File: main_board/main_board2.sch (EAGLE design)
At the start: 16 parts, among them J1 Bar30, J2 Temp/Hum, J3 LED, Q1 MOSFET, Q2 MOSFET, Q3 MOSFET

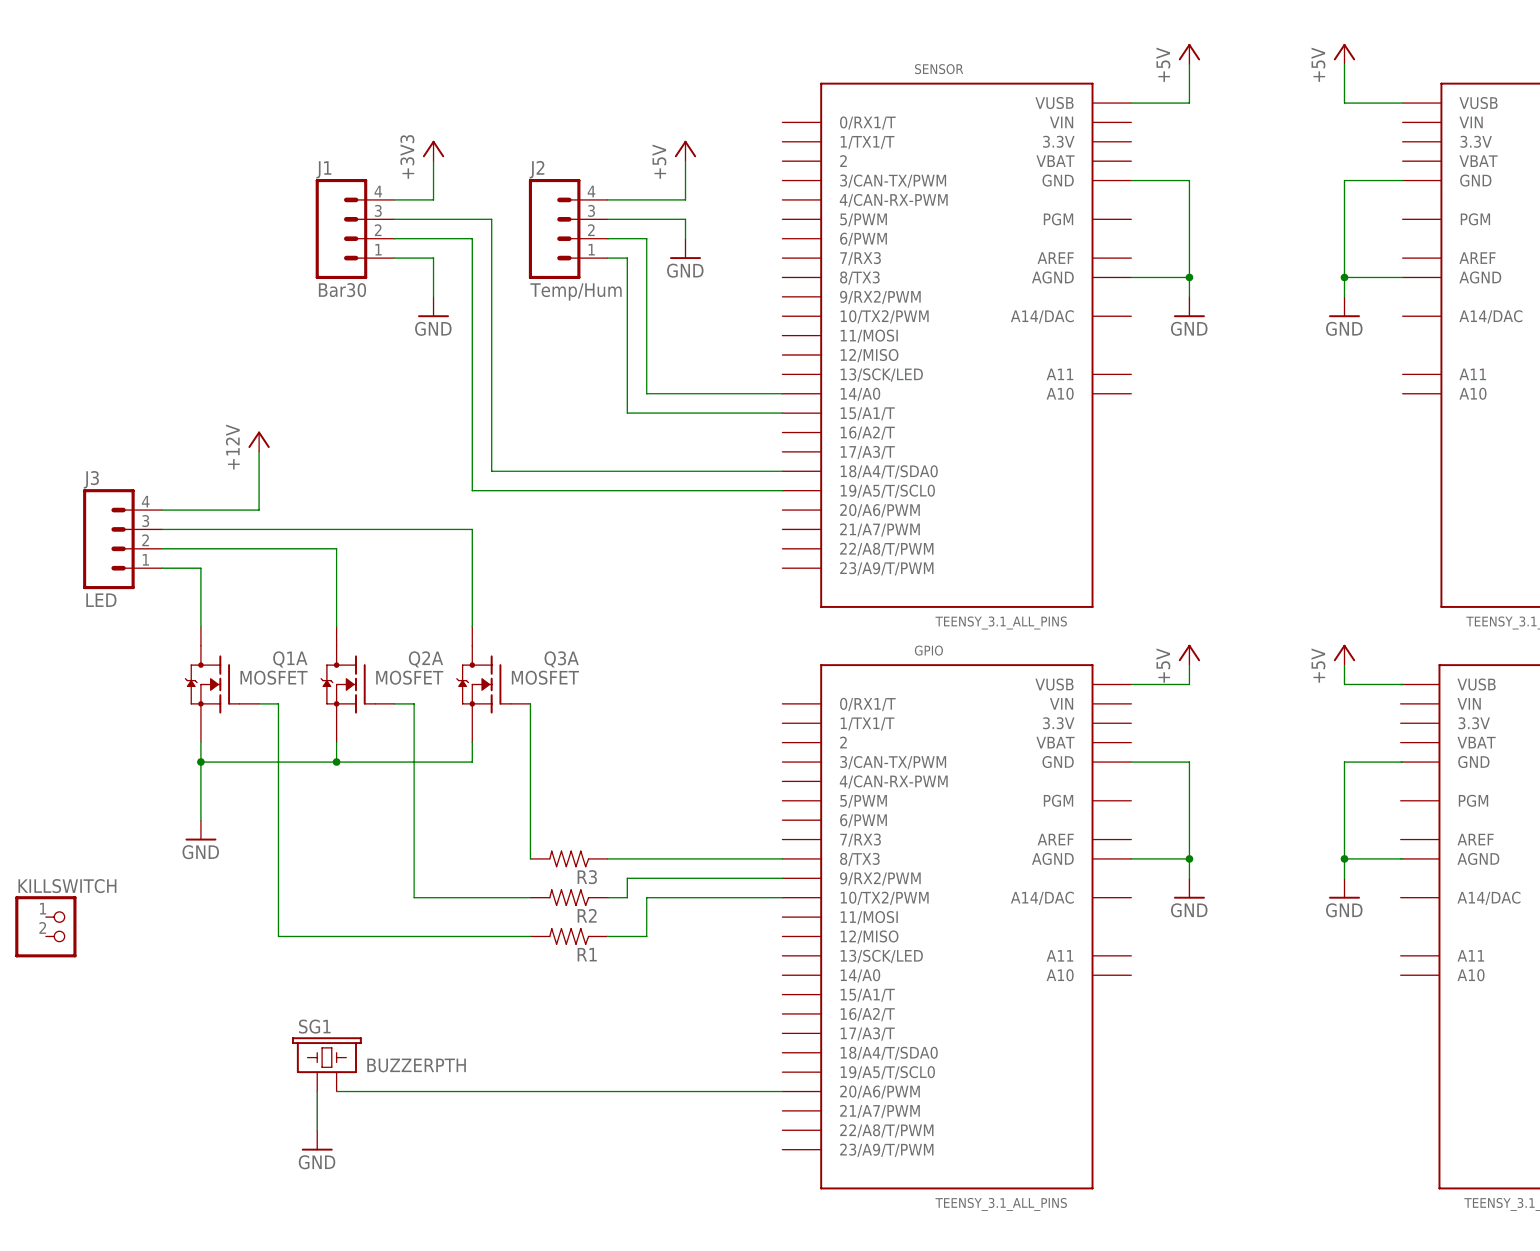
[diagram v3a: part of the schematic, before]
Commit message: added kill switch. moved minor parts around. added 3.3V references
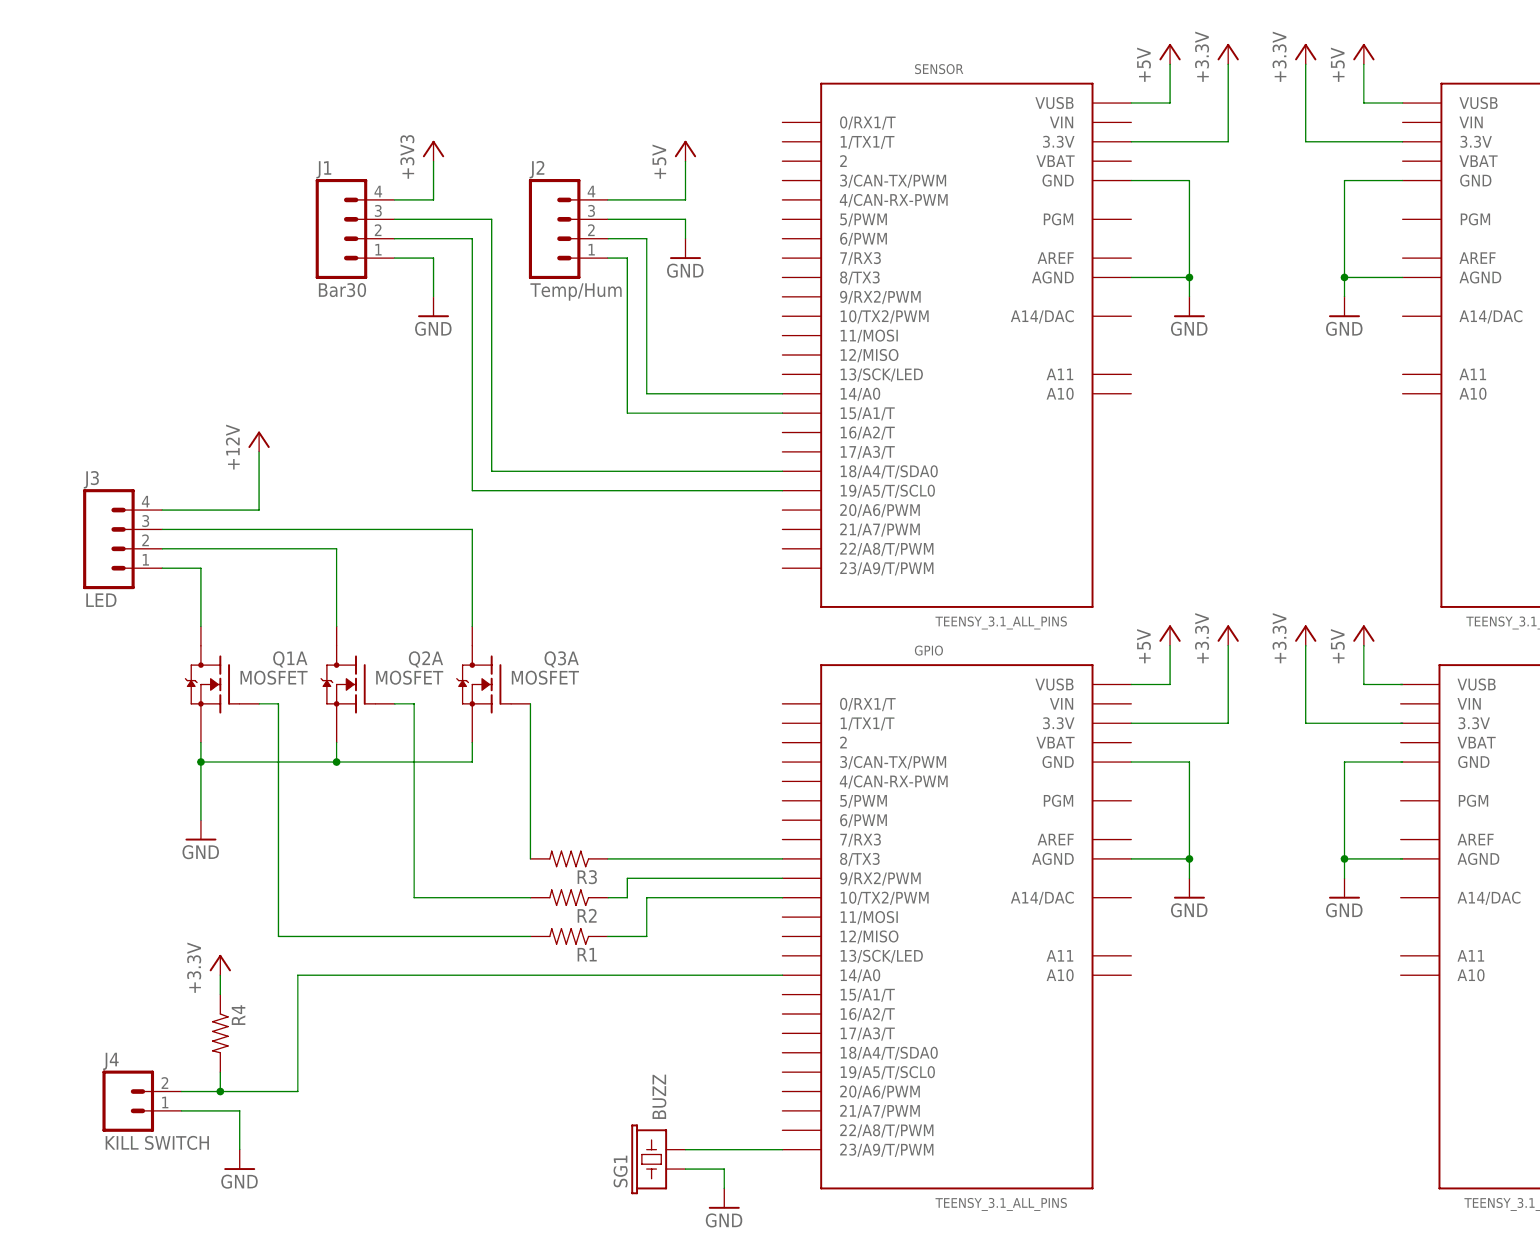
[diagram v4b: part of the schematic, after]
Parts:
- removed KILLSWITCH: (no value), pinhead:PINHD-1X2
- added J4: KILL SWITCH, SparkFun-Connectors:M02PTH
- added R4: (no value), SparkFun-Resistors:RESISTORPTH-1/4W
- SG1: value BUZZERPTH -> BUZZ
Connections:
- new net N$20: GPIO.14/A0, J4.2, R4.2
- net +5V: now also GPIO.3.3V, POWER.3.3V, R4.1, SENSOR.3.3V
- net GND: now also J4.1
- net N$13: now also GPIO.23/A9/T/PWM; no longer GPIO.20/A6/PWM
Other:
- moved on the sheet: SG1
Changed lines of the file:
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@@
 <part name="GND1" library="supply1" deviceset="GND" device=""/>
 <part name="P+1" library="supply1" deviceset="+5V" device=""/>
-<part name="KILLSWITCH" library="pinhead" deviceset="PINHD-1X2" device=""/>
 <part name="J1" library="SparkFun-Connectors" deviceset="M04" device="PTH" value="Bar30"/>
-<part name="SG1" library="SparkFun-Electromechanical" deviceset="BUZZER" device="PTH"/>
+<part name="SG1" library="SparkFun-Electromechanical" deviceset="BUZZER" device="PTH" value="BUZZ"/>
 <part name="GND2" library="SparkFun-Aesthetics" deviceset="GND" device=""/>
 <part name="GND3" library="SparkFun-Aesthetics" deviceset="GND" device=""/>
@@
 <part name="GND7" library="supply1" deviceset="GND" device=""/>
 <part name="GND8" library="supply1" deviceset="GND" device=""/>
+<part name="J4" library="SparkFun-Connectors" deviceset="M02" device="PTH" value="KILL SWITCH"/>
+<part name="R4" library="SparkFun-Resistors" deviceset="RESISTOR" device="PTH-1/4W"/>
+<part name="GND9" library="supply1" deviceset="GND" device=""/>
+<part name="+3.3V" library="supply1" deviceset="+5V" device="" value="+3.3V"/>
+<part name="+3.3V1" library="supply1" deviceset="+5V" device="" value="+3.3V"/>
+<part name="+3.3V2" library="supply1" deviceset="+5V" device="" value="+3.3V"/>
+<part name="+3.3V3" library="supply1" deviceset="+5V" device="" value="+3.3V"/>
+<part name="+3.3V4" library="supply1" deviceset="+5V" device="" value="+3.3V"/>
 </parts>
 <sheets>
@@
 <instance part="THRUSTER" gate="G$1" x="60.706" y="53.34" rot="MR0"/>
 <instance part="GND1" gate="1" x="10.16" y="132.08"/>
-<instance part="P+1" gate="1" x="10.16" y="167.64"/>
-<instance part="KILLSWITCH" gate="G$1" x="-137.16" y="50.8"/>
+<instance part="P+1" gate="1" x="7.62" y="167.64"/>
 <instance part="J1" gate="G$1" x="-99.06" y="142.24"/>
-<instance part="SG1" gate="G$1" x="-104.14" y="33.02"/>
-<instance part="GND2" gate="1" x="-104.14" y="22.86"/>
+<instance part="SG1" gate="G$1" x="-58.42" y="20.32" rot="R90"/>
+<instance part="GND2" gate="1" x="-50.8" y="15.24"/>
 <instance part="GND3" gate="1" x="-88.9" y="132.08"/>
 <instance part="+3V1" gate="G$1" x="-88.9" y="154.94"/>
@@
 <instance part="P+3" gate="1" x="-111.76" y="116.84"/>
 <instance part="JP1" gate="A" x="121.92" y="55.88"/>
-<instance part="P+4" gate="1" x="30.48" y="167.64"/>
-<instance part="P+5" gate="1" x="30.48" y="88.9"/>
-<instance part="P+6" gate="1" x="10.16" y="88.9"/>
+<instance part="P+4" gate="1" x="33.02" y="167.64"/>
+<instance part="P+5" gate="1" x="33.02" y="91.44"/>
+<instance part="P+6" gate="1" x="7.62" y="91.44"/>
 <instance part="GND6" gate="1" x="30.48" y="132.08"/>
 <instance part="GND7" gate="1" x="30.48" y="55.88"/>
 <instance part="GND8" gate="1" x="10.16" y="55.88"/>
+<instance part="J4" gate="G$1" x="-129.54" y="27.94"/>
+<instance part="R4" gate="G$1" x="-116.84" y="38.1" rot="R270"/>
+<instance part="GND9" gate="1" x="-114.3" y="20.32"/>
+<instance part="+3.3V" gate="1" x="-116.84" y="48.26"/>
+<instance part="+3.3V1" gate="1" x="15.24" y="91.44"/>
+<instance part="+3.3V2" gate="1" x="25.4" y="91.44"/>
+<instance part="+3.3V3" gate="1" x="15.24" y="167.64"/>
+<instance part="+3.3V4" gate="1" x="25.4" y="167.64"/>
 </instances>
 <busses>
@@
 <nets>
 <net name="GND" class="0">
-<segment>
-<pinref part="SG1" gate="G$1" pin="1"/>
-<pinref part="GND2" gate="1" pin="GND"/>
-<wire x1="-104.14" y1="30.48" x2="-104.14" y2="25.4" width="0.1524" layer="91"/>
-</segment>
 <segment>
 <pinref part="J1" gate="G$1" pin="1"/>
@@
 <junction x="30.48" y="137.16"/>
 </segment>
+<segment>
+<pinref part="GND2" gate="1" pin="GND"/>
+<wire x1="-50.8" y1="17.78" x2="-50.8" y2="20.32" width="0.1524" layer="91"/>
+<pinref part="SG1" gate="G$1" pin="1"/>
+<wire x1="-50.8" y1="20.32" x2="-55.88" y2="20.32" width="0.1524" layer="91"/>
+</segment>
+<segment>
+<pinref part="GND9" gate="1" pin="GND"/>
+<wire x1="-114.3" y1="22.86" x2="-114.3" y2="27.94" width="0.1524" layer="91"/>
+<pinref part="J4" gate="G$1" pin="1"/>
+<wire x1="-114.3" y1="27.94" x2="-121.92" y2="27.94" width="0.1524" layer="91"/>
+</segment>
 </net>
 <net name="N$1" class="0">
@@
 <pinref part="SENSOR" gate="G$1" pin="VUSB"/>
 <pinref part="P+1" gate="1" pin="+5V"/>
-<wire x1="2.54" y1="160.02" x2="10.16" y2="160.02" width="0.1524" layer="91"/>
-<wire x1="10.16" y1="160.02" x2="10.16" y2="165.1" width="0.1524" layer="91"/>
+<wire x1="2.54" y1="160.02" x2="7.62" y2="160.02" width="0.1524" layer="91"/>
+<wire x1="7.62" y1="160.02" x2="7.62" y2="165.1" width="0.1524" layer="91"/>
 </segment>
 <segment>
 <pinref part="GPIO" gate="G$1" pin="VUSB"/>
 <pinref part="P+6" gate="1" pin="+5V"/>
-<wire x1="2.54" y1="83.82" x2="10.16" y2="83.82" width="0.1524" layer="91"/>
-<wire x1="10.16" y1="83.82" x2="10.16" y2="86.36" width="0.1524" layer="91"/>
+<wire x1="2.54" y1="83.82" x2="7.62" y2="83.82" width="0.1524" layer="91"/>
+<wire x1="7.62" y1="83.82" x2="7.62" y2="88.9" width="0.1524" layer="91"/>
 </segment>
 <segment>
 <pinref part="P+5" gate="1" pin="+5V"/>
-<wire x1="30.48" y1="86.36" x2="30.48" y2="83.82" width="0.1524" layer="91"/>
-<wire x1="30.48" y1="83.82" x2="38.1" y2="83.82" width="0.1524" layer="91"/>
+<wire x1="33.02" y1="88.9" x2="33.02" y2="83.82" width="0.1524" layer="91"/>
+<wire x1="33.02" y1="83.82" x2="38.1" y2="83.82" width="0.1524" layer="91"/>
 </segment>
 <segment>
 <pinref part="POWER" gate="G$1" pin="VUSB"/>
 <pinref part="P+4" gate="1" pin="+5V"/>
-<wire x1="38.1" y1="160.02" x2="30.48" y2="160.02" width="0.1524" layer="91"/>
-<wire x1="30.48" y1="160.02" x2="30.48" y2="165.1" width="0.1524" layer="91"/>
+<wire x1="38.1" y1="160.02" x2="33.02" y2="160.02" width="0.1524" layer="91"/>
+<wire x1="33.02" y1="160.02" x2="33.02" y2="165.1" width="0.1524" layer="91"/>
+</segment>
+<segment>
+<pinref part="R4" gate="G$1" pin="1"/>
+<pinref part="+3.3V" gate="1" pin="+5V"/>
+<wire x1="-116.84" y1="43.18" x2="-116.84" y2="45.72" width="0.1524" layer="91"/>
+</segment>
+<segment>
+<pinref part="GPIO" gate="G$1" pin="3.3V"/>
+<pinref part="+3.3V1" gate="1" pin="+5V"/>
+<wire x1="2.54" y1="78.74" x2="15.24" y2="78.74" width="0.1524" layer="91"/>
+<wire x1="15.24" y1="78.74" x2="15.24" y2="88.9" width="0.1524" layer="91"/>
+</segment>
+<segment>
+<pinref part="+3.3V2" gate="1" pin="+5V"/>
+<wire x1="38.1" y1="78.74" x2="25.4" y2="78.74" width="0.1524" layer="91"/>
+<wire x1="25.4" y1="78.74" x2="25.4" y2="88.9" width="0.1524" layer="91"/>
+</segment>
+<segment>
+<pinref part="+3.3V3" gate="1" pin="+5V"/>
+<wire x1="15.24" y1="154.94" x2="15.24" y2="165.1" width="0.1524" layer="91"/>
+<pinref part="SENSOR" gate="G$1" pin="3.3V"/>
+<wire x1="2.54" y1="154.94" x2="15.24" y2="154.94" width="0.1524" layer="91"/>
+</segment>
+<segment>
+<pinref part="+3.3V4" gate="1" pin="+5V"/>
+<wire x1="25.4" y1="154.94" x2="25.4" y2="165.1" width="0.1524" layer="91"/>
+<pinref part="POWER" gate="G$1" pin="3.3V"/>
+<wire x1="25.4" y1="154.94" x2="38.1" y2="154.94" width="0.1524" layer="91"/>
 </segment>
 </net>
@@
 </segment>
 </net>
-<net name="N$13" class="0">
-<segment>
-<pinref part="GPIO" gate="G$1" pin="20/A6/PWM"/>
-<wire x1="-101.6" y1="30.48" x2="-43.18" y2="30.48" width="0.1524" layer="91"/>
-<pinref part="SG1" gate="G$1" pin="2"/>
-</segment>
-</net>
 <net name="N$12" class="0">
 <segment>
@@
 </segment>
 </net>
+<net name="N$13" class="0">
+<segment>
+<pinref part="SG1" gate="G$1" pin="2"/>
+<pinref part="GPIO" gate="G$1" pin="23/A9/T/PWM"/>
+<wire x1="-55.88" y1="22.86" x2="-43.18" y2="22.86" width="0.1524" layer="91"/>
+</segment>
+</net>
+<net name="N$20" class="0">
+<segment>
+<pinref part="J4" gate="G$1" pin="2"/>
+<wire x1="-121.92" y1="30.48" x2="-116.84" y2="30.48" width="0.1524" layer="91"/>
+<pinref part="R4" gate="G$1" pin="2"/>
+<wire x1="-116.84" y1="30.48" x2="-116.84" y2="33.02" width="0.1524" layer="91"/>
+<pinref part="GPIO" gate="G$1" pin="14/A0"/>
+<wire x1="-43.18" y1="45.72" x2="-106.68" y2="45.72" width="0.1524" layer="91"/>
+<wire x1="-106.68" y1="45.72" x2="-106.68" y2="30.48" width="0.1524" layer="91"/>
+<wire x1="-106.68" y1="30.48" x2="-116.84" y2="30.48" width="0.1524" layer="91"/>
+<junction x="-116.84" y="30.48"/>
+</segment>
+</net>
